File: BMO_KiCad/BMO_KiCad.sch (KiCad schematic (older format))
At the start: 27 parts

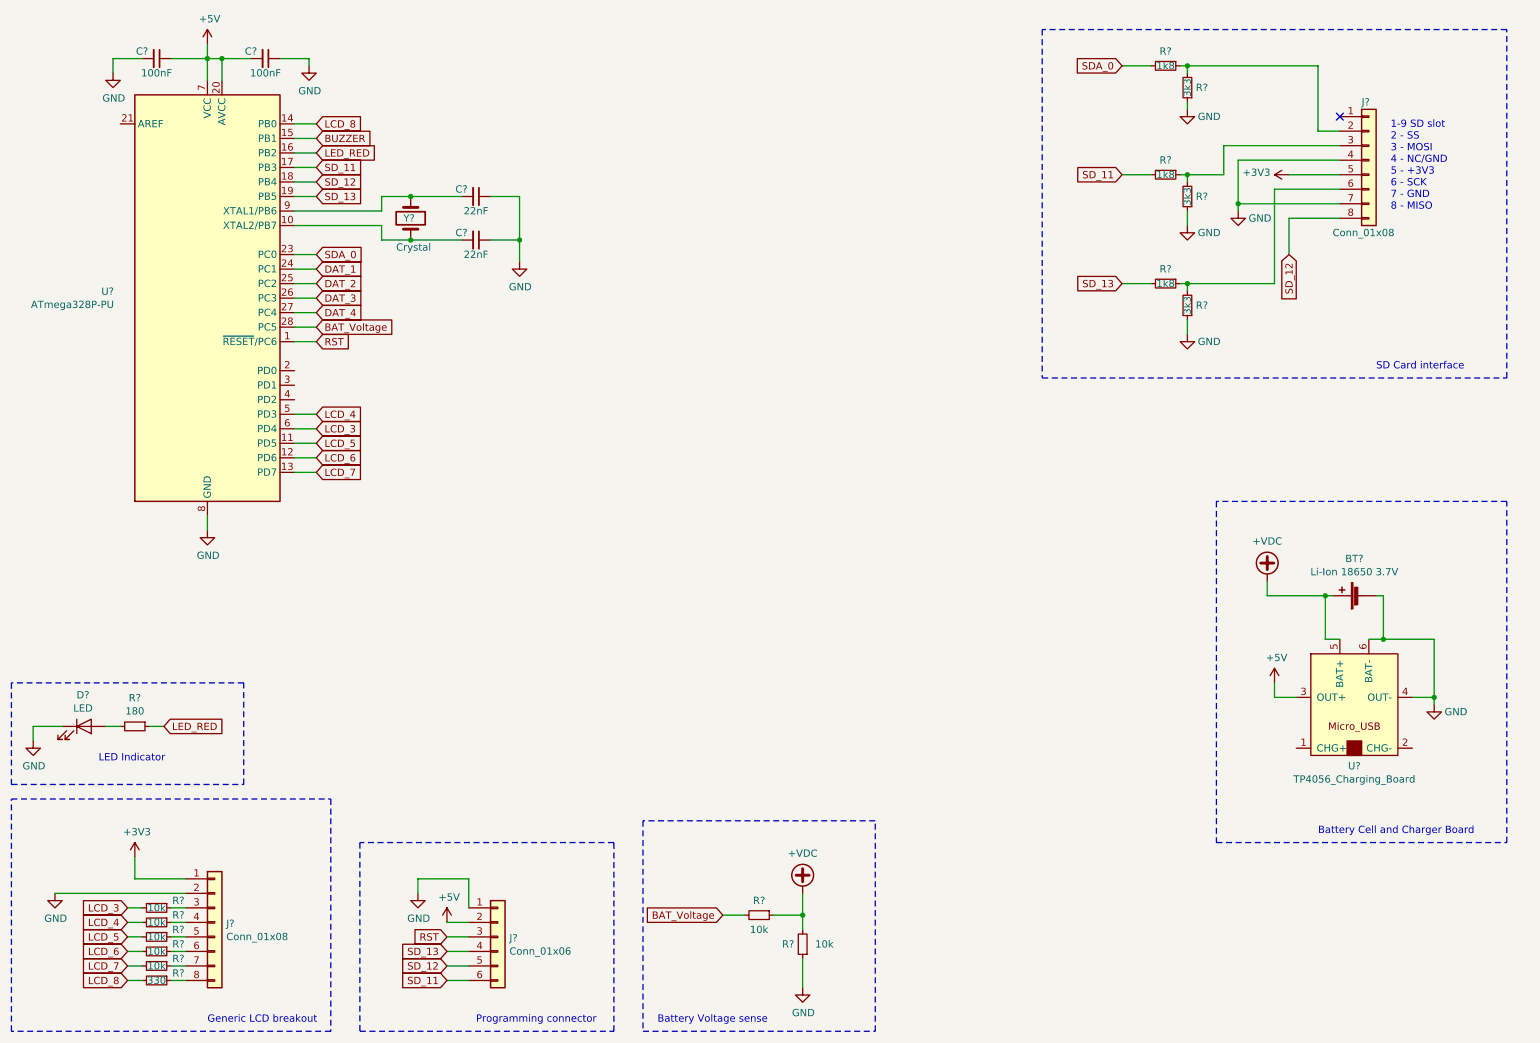
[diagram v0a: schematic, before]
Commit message: Kicad updates
Resolved sd card pinout
Added Amplifier board
Added 3v3 regulator
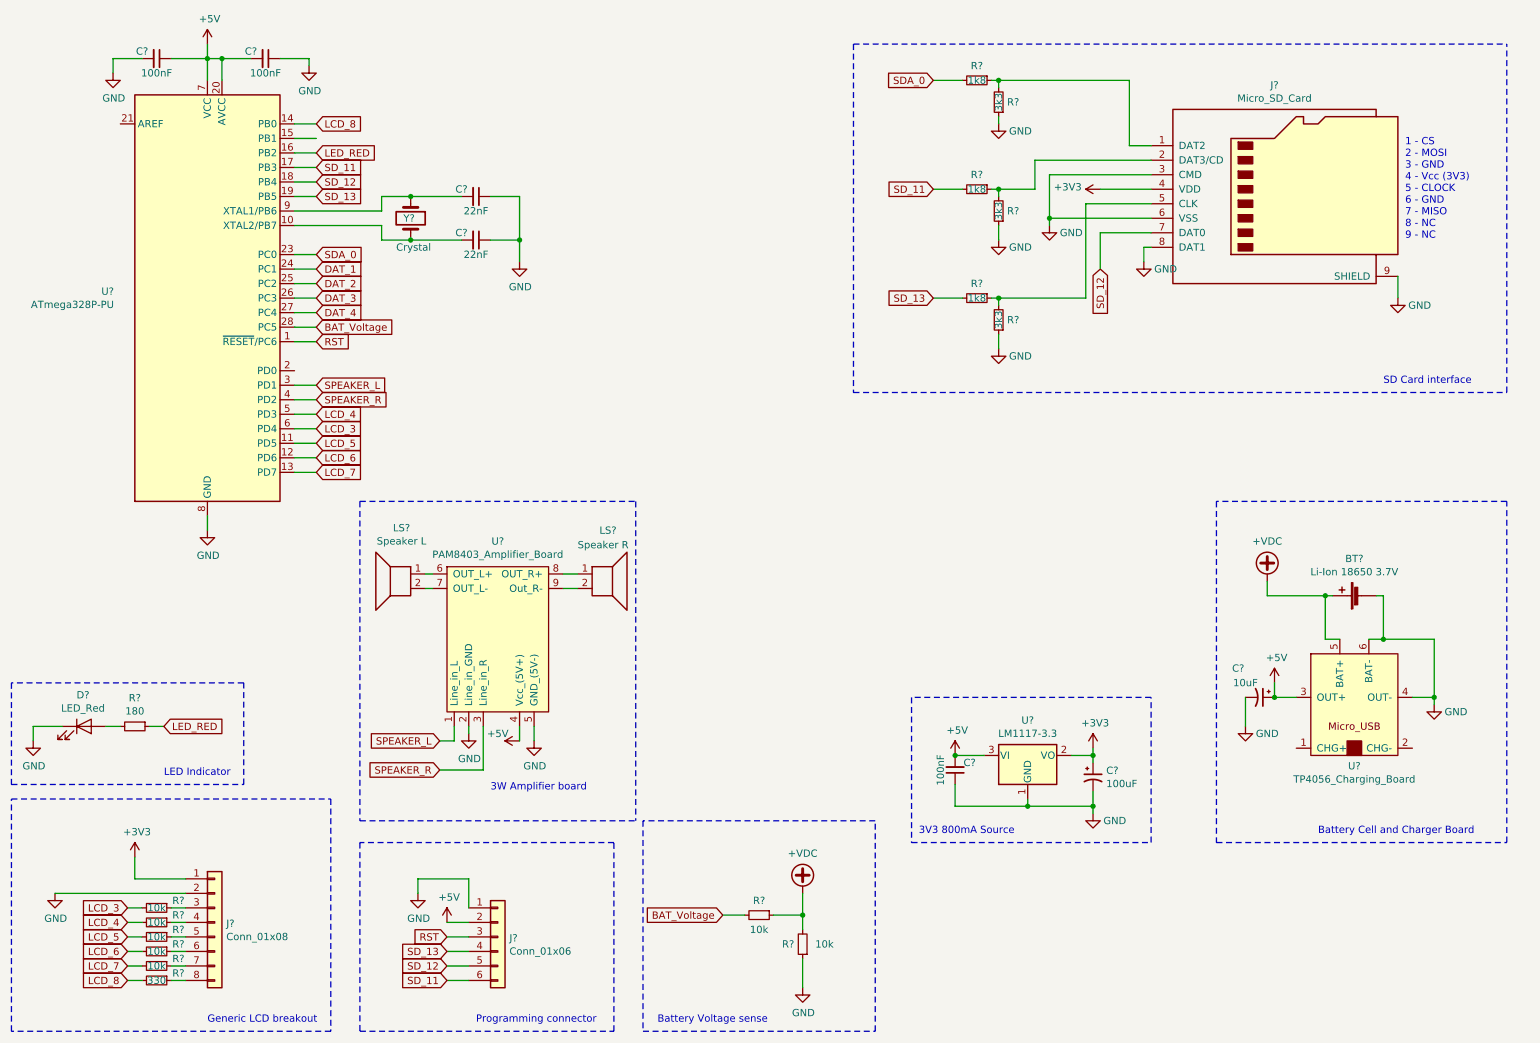
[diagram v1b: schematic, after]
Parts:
- removed J?: Conn_01x08, symbol Connector_Generic:Conn_01x08
- added C?: 100uF, Capacitor_Tantalum_SMD:CP_EIA-1608-10_AVX-L, symbol Device:CP1_Small
- added C?: 10uF, Capacitor_Tantalum_SMD:CP_EIA-1608-10_AVX-L, symbol Device:CP1_Small
- added C?: 100nF, symbol Device:C_Small
- added J?: Micro_SD_Card, Connector_Card:microSD_HC_Molex_104031-0811, symbol Connector:Micro_SD_Card
- added LS?: Speaker L, symbol Device:Speaker
- added LS?: Speaker R, symbol Device:Speaker
- added U?: LM1117-3.3, Package_TO_SOT_SMD:SOT-223-3_TabPin2, symbol Regulator_Linear:LM1117-3.3
- added U?: PAM8403_Amplifier_Board, symbol _DV_SymLib:PAM8403_Amplifier_Board
- D?: value LED -> LED_Red; footprint (none) -> LED_SMD:LED_0603_1608Metric
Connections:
- net +3V3: now also C?.1, J?.4 (VDD), U?.2 (VO)
- net +5V: now also C?.1, C?.2, U?.3 (VI), U?.4 (Vcc_(5V+))
- net GND: now also C?.1, C?.2, C?.2, J?.3 (CMD), J?.6 (VSS), J?.8 (DAT1), J?.9 (SHIELD), U?.1 (GND), U?.2 (Line_in_GND), U?.5 (GND_(5V-))
- net SD_12: now also J?.7 (DAT0)
- net SPEAKER_L: now reaches U?.3 (PD1)
- net SPEAKER_L: now also U?.1 (Line_in_L)
- net SPEAKER_R: now reaches U?.4 (PD2)
- net SPEAKER_R: now also U?.3 (Line_in_R)
- net at R?.1, R?.2: now also J?.1 (DAT2)
- net at R?.1, R?.2: now also J?.2 (DAT3/CD)
- net at R?.1, R?.2: now also J?.5 (CLK)
- net BUZZER: no longer names the net of U?.15 (PB1)
- new net: LS?.1, U?.6 (OUT_L+)
- new net: LS?.2, U?.7 (OUT_L-)
- new net: LS?.1, U?.8 (OUT_R+)
- new net: LS?.2, U?.9 (Out_R-)
- no-connect marks 1 -> 0
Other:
- note added: "1 - CS\n2 - MOSI\n3 - GND\n4 - Vcc (3V3)\n5 - CLOCK\n6 - GND\n7 - MISO\n8 - NC\n9 - NC"
- note added: "3V3 800mA Source"
- note added: "3W Amplifier board"
- note removed: "1-9 SD slot\n2 - SS\n3 - MOSI\n4 - NC/GND\n5 - +3V3\n6 - SCK\n7 - GND\n8 - MISO"
- moved on the sheet: R?
